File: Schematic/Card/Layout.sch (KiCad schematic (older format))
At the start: 27 parts, among them J1 JTAG, J2 Power, U1 RF430FRL

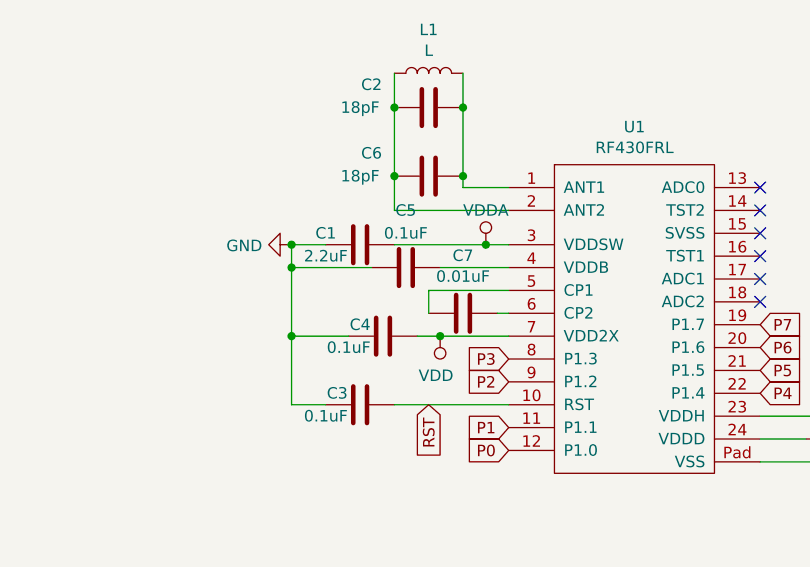
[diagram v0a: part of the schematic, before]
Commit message: Fixed ground issue and cleaned up board
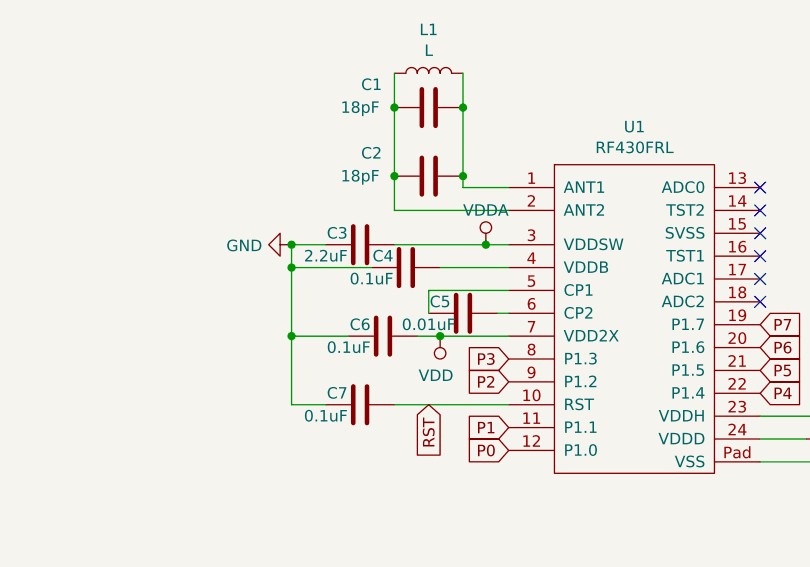
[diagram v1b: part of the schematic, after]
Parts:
- renumbered C2 to C1, C6 to C2, C1 to C3, C5 to C4, C7 to C5, C4 to C6, C3 to C7
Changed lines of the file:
@@
 $EndComp
 $Comp
-L Device:C C2
+L Device:C C1
 U 1 1 5C18D9DC
 P 7450 1950
-F 0 "C2" V 7350 1700 50  0000 C CNN
+F 0 "C1" V 7350 1700 50  0000 C CNN
 F 1 "18pF" V 7450 1650 50  0000 C CNN
 F 2 "Capacitors_SMD:C_0805" H 7488 1800 50  0001 C CNN
@@
 	7600 2300 7600 2250
 $Comp
-L Device:C C1
+L Device:C C3
 U 1 1 5C18DACD
 P 7150 2550
-F 0 "C1" V 7100 2400 50  0000 C CNN
+F 0 "C3" V 7100 2450 50  0000 C CNN
 F 1 "2.2uF" V 7200 2400 50  0000 C CNN
 F 2 "Capacitors_SMD:C_0805" H 7188 2400 50  0001 C CNN
@@
 $EndComp
 $Comp
-L Device:C C5
+L Device:C C4
 U 1 1 5C18DBC1
 P 7350 2650
-F 0 "C5" V 7100 2650 50  0000 C CNN
-F 1 "0.1uF" V 7200 2650 50  0000 C CNN
+F 0 "C4" V 7300 2550 50  0000 C CNN
+F 1 "0.1uF" V 7400 2500 50  0000 C CNN
 F 2 "Capacitors_SMD:C_0805" H 7388 2500 50  0001 C CNN
 F 3 "~" H 7350 2650 50  0001 C CNN
@@
 	7500 2650 7800 2650
 $Comp
-L Device:C C7
+L Device:C C5
 U 1 1 5C18DD20
 P 7600 2850
-F 0 "C7" V 7348 2850 50  0000 C CNN
-F 1 "0.01uF" V 7439 2850 50  0000 C CNN
+F 0 "C5" V 7550 2750 50  0000 C CNN
+F 1 "0.01uF" V 7650 2700 50  0000 C CNN
 F 2 "Capacitors_SMD:C_0805" H 7638 2700 50  0001 C CNN
 F 3 "~" H 7600 2850 50  0001 C CNN
@@
 	7450 2750 7450 2850
 $Comp
-L Device:C C4
+L Device:C C6
 U 1 1 5C18DE93
 P 7250 2950
-F 0 "C4" V 7200 2850 50  0000 C CNN
+F 0 "C6" V 7200 2850 50  0000 C CNN
 F 1 "0.1uF" V 7300 2800 50  0000 C CNN
 F 2 "Capacitors_SMD:C_0805" H 7288 2800 50  0001 C CNN
@@
 $EndComp
 $Comp
-L Device:C C3
+L Device:C C7
 U 1 1 5C18E108
 P 7150 3250
-F 0 "C3" V 7100 3150 50  0000 C CNN
+F 0 "C7" V 7100 3150 50  0000 C CNN
 F 1 "0.1uF" V 7200 3100 50  0000 C CNN
 F 2 "Capacitors_SMD:C_0805" H 7188 3100 50  0001 C CNN
@@
 Connection ~ 7300 1950
 $Comp
-L Device:C C6
+L Device:C C2
 U 1 1 5C18ED62
 P 7450 2250
-F 0 "C6" V 7350 2000 50  0000 C CNN
+F 0 "C2" V 7350 2000 50  0000 C CNN
 F 1 "18pF" V 7450 1950 50  0000 C CNN
 F 2 "Capacitors_SMD:C_0805" H 7488 2100 50  0001 C CNN

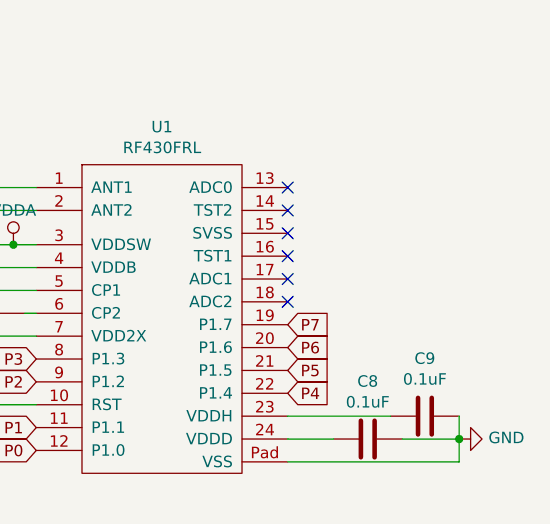
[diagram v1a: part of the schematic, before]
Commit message: V3, changes may improve reading distance
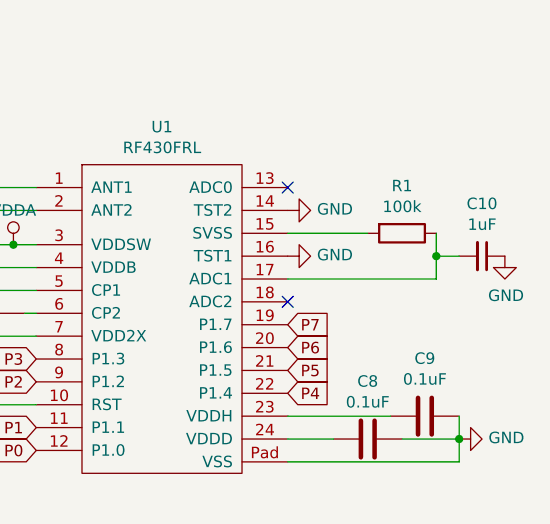
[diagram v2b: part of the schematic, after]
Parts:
- added C10: 1uF, Capacitors_SMD:C_0805, symbol Device:C_Small
- added R1: 100k, Resistors_SMD:R_0805, symbol Device:R
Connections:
- net GND: now also U1.14 (TST2), U1.16 (TST1), C10.1
- net at U1.15 (SVSS): now also R1.2
- net at U1.17 (ADC1): now also C10.2, R1.1
- no-connect marks 6 -> 2
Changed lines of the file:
@@
 P6
 NoConn ~ 8900 2300
-NoConn ~ 8900 2400
-NoConn ~ 8900 2500
-NoConn ~ 8900 2600
-NoConn ~ 8900 2700
 NoConn ~ 8900 2800
 Connection ~ 1300 5850
@@
 	0    1    1    0
 $EndComp
+$Comp
+L power:GND #PWR09
+U 1 1 5C6D0788
+P 8900 2400
+F 0 "#PWR09" H 8900 2150 50  0001 C CNN
+F 1 "GND" V 8905 2272 50  0000 R CNN
+F 2 "" H 8900 2400 50  0001 C CNN
+F 3 "" H 8900 2400 50  0001 C CNN
+	1    8900 2400
+	0    -1   -1   0
+$EndComp
+$Comp
+L power:GND #PWR011
+U 1 1 5C6D088B
+P 8900 2600
+F 0 "#PWR011" H 8900 2350 50  0001 C CNN
+F 1 "GND" V 8905 2472 50  0000 R CNN
+F 2 "" H 8900 2600 50  0001 C CNN
+F 3 "" H 8900 2600 50  0001 C CNN
+	1    8900 2600
+	0    -1   -1   0
+$EndComp
+$Comp
+L Device:R R1
+U 1 1 5C6D0A2F
+P 9400 2500
+F 0 "R1" V 9193 2500 50  0000 C CNN
+F 1 "100k" V 9284 2500 50  0000 C CNN
+F 2 "Resistors_SMD:R_0805" V 9330 2500 50  0001 C CNN
+F 3 "~" H 9400 2500 50  0001 C CNN
+	1    9400 2500
+	0    1    1    0
+$EndComp
+Wire Wire Line
+	8900 2500 9250 2500
+Wire Wire Line
+	8900 2700 9550 2700
+Wire Wire Line
+	9550 2700 9550 2600
+$Comp
+L Device:C_Small C10
+U 1 1 5C6D3305
+P 9750 2600
+F 0 "C10" V 9521 2600 50  0000 C CNN
+F 1 "1uF" V 9612 2600 50  0000 C CNN
+F 2 "Capacitors_SMD:C_0805" H 9750 2600 50  0001 C CNN
+F 3 "~" H 9750 2600 50  0001 C CNN
+	1    9750 2600
+	0    1    1    0
+$EndComp
+Wire Wire Line
+	9550 2600 9650 2600
+Connection ~ 9550 2600
+Wire Wire Line
+	9550 2600 9550 2500
+$Comp
+L power:GND #PWR012
+U 1 1 5C6D48D9
+P 9850 2600
+F 0 "#PWR012" H 9850 2350 50  0001 C CNN
+F 1 "GND" H 9855 2427 50  0000 C CNN
+F 2 "" H 9850 2600 50  0001 C CNN
+F 3 "" H 9850 2600 50  0001 C CNN
+	1    9850 2600
+	1    0    0    -1
+$EndComp
 $EndSCHEMATC
